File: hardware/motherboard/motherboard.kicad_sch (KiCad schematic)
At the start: 82 parts, among them J1 IMU Connector, J2 JST-VH, J3 JST-VH, J4 JST-PH, J5 USB C 2.0, Q1 TSM7P06CP_ROG, Q2 TSM7P06CP_ROG, SW1 A, SW10 Right, SW11 Left, SW12 Up, SW13 Reset, SW2 B, SW3 X, SW4 Y, SW5 LB, SW6 RB, SW7 Start, SW8 Select, SW9 Down, U1 ESP32-S3-WROOM-1, U2 MCP73831-2-OT, U3 TPS75533KTTRG3, U4 TLV75709PDBV, U5 COM-09032

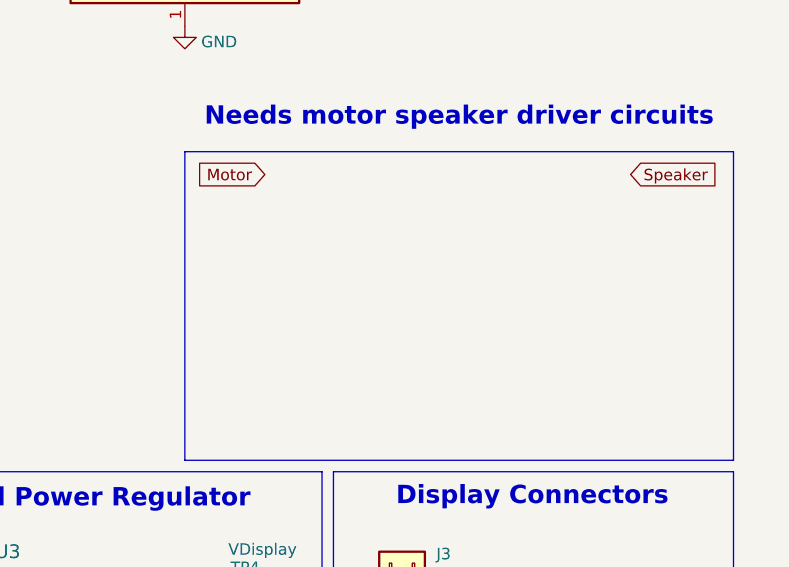
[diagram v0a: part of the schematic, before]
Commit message: Updated Schematic, Added motor/speaker connector
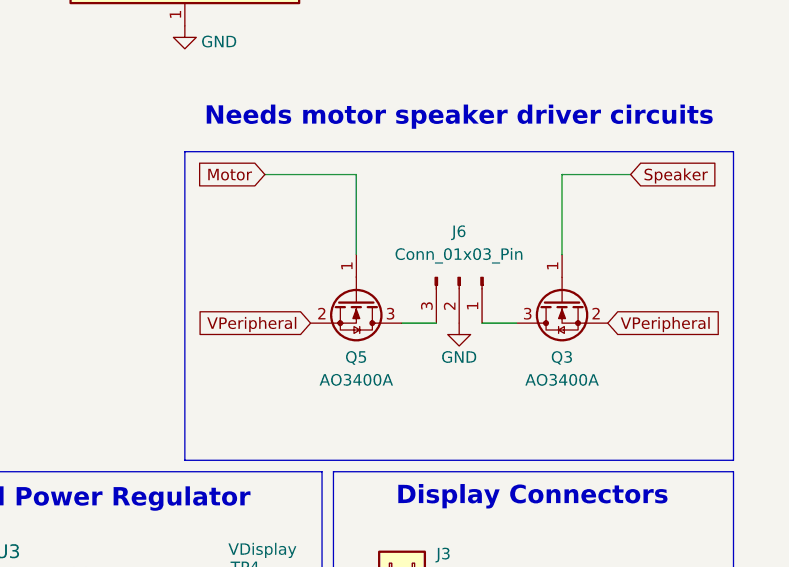
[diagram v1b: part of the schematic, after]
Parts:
- added J6: Conn_01x03_Pin, symbol Connector:Conn_01x03_Pin
- added Q3, Q5: AO3400A, Package_TO_SOT_SMD:SOT-23, symbol Transistor_FET:AO3400A
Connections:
- net GND: now also J6.2 (Pin_2)
- net Motor: now also Q5.1 (G)
- net Speaker: now also Q3.1 (G)
- net VPeripheral: now also Q3.2 (S), Q5.2 (S)
- new net: J6.1 (Pin_1), Q3.3 (D)
- new net: J6.3 (Pin_3), Q5.3 (D)

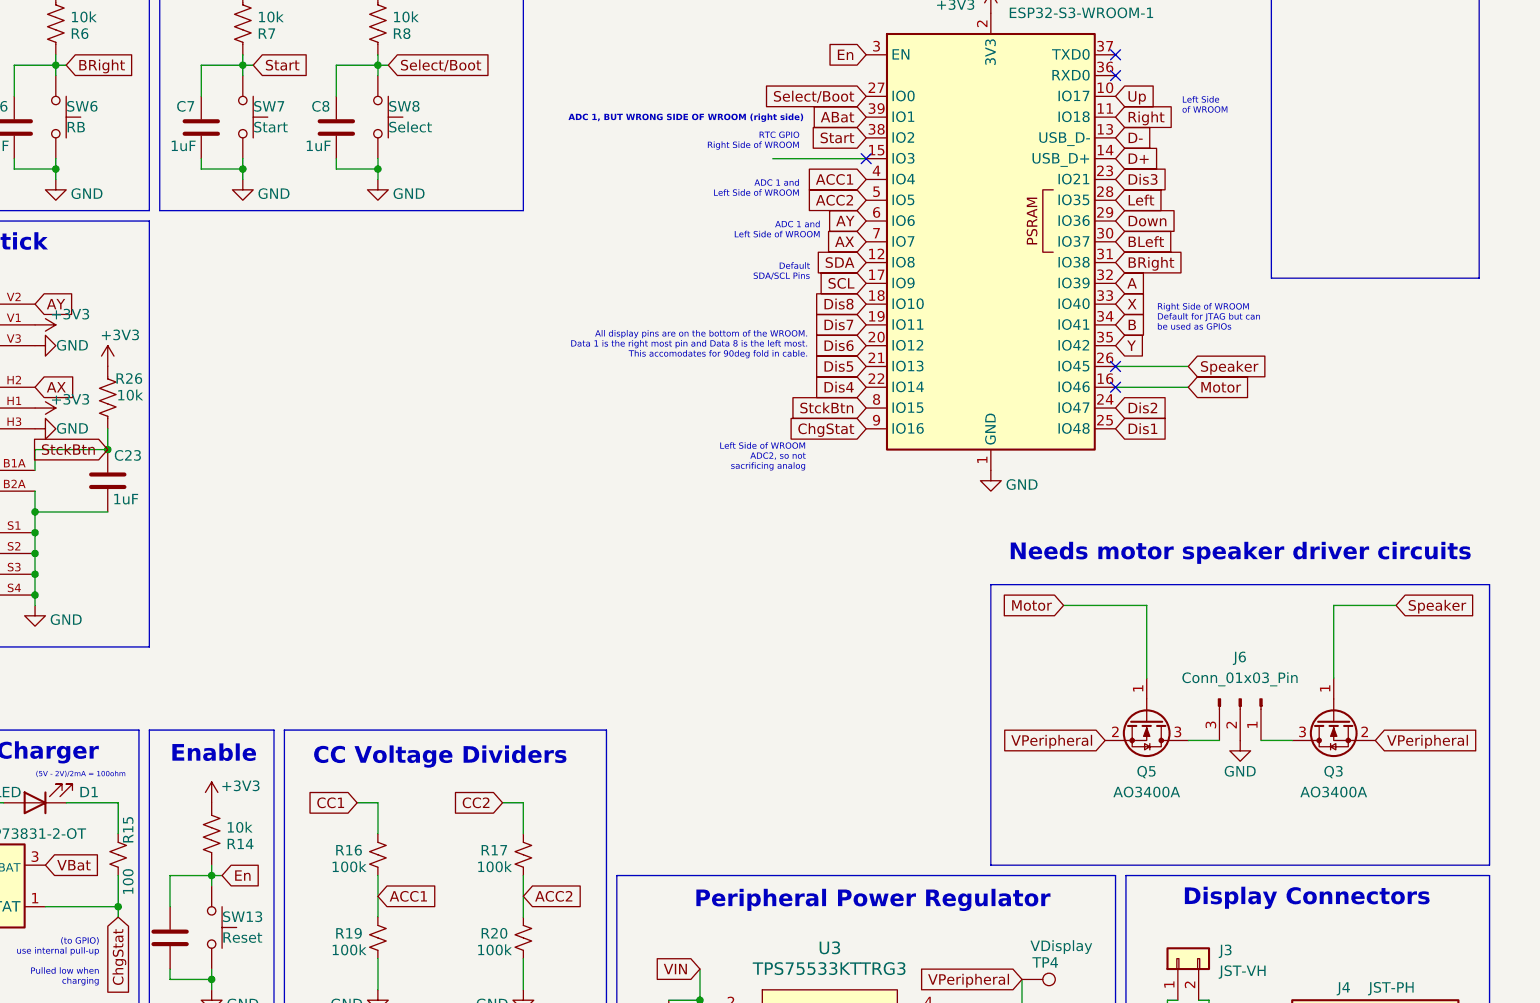
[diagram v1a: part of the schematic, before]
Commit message: Added ucbc 3d model
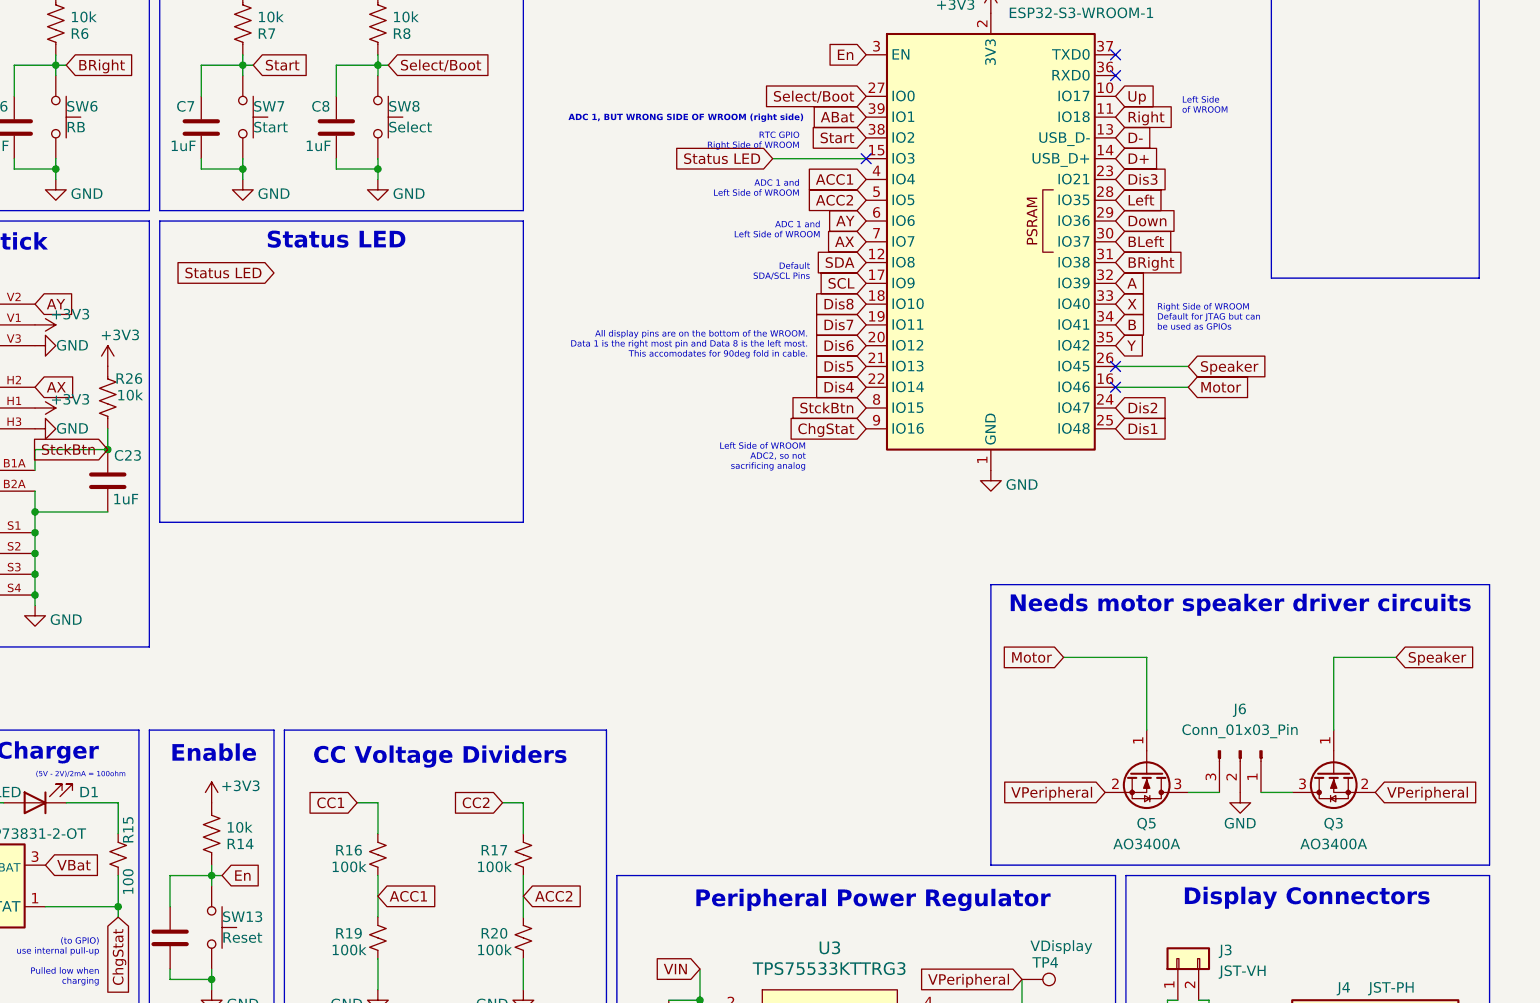
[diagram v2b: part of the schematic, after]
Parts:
- J6: footprint (none) -> Connector_JST:JST_EH_S3B-EH_1x03_P2.50mm_Horizontal
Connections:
- net Status LED: now reaches U1.15 (IO3)
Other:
- note added: "Status LED"
- moved on the sheet: J6, Q3, Q5
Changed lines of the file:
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@@
 	)
 	(rectangle
+		(start 120.65 50.8)
+		(end 165.1 87.63)
+		(stroke
+			(width 0)
+			(type default)
+		)
+		(fill
+			(type none)
+		)
+	)
+	(rectangle
 		(start 81.28 12.7)
 		(end 119.38 49.53)
@@
 	(text "Needs motor speaker driver circuits"
 		(exclude_from_sim no)
-		(at 252.73 91.44 0)
+		(at 252.73 97.79 0)
 		(effects
 			(font
@@
 		)
 	)
+	(text "Status LED"
+		(exclude_from_sim no)
+		(at 142.24 53.34 0)
+		(effects
+			(font
+				(size 2.032 2.032)
+				(thickness 0.6096)
+				(bold yes)
+			)
+		)
+	)
 	(junction
 		(at 127 130.81)
@@
 	(wire
 		(pts
-			(xy 264.16 97.79) (xy 264.16 106.68)
+			(xy 264.16 104.14) (xy 264.16 113.03)
 		)
 		(stroke
@@
 	(wire
 		(pts
-			(xy 255.27 114.3) (xy 259.08 114.3)
+			(xy 255.27 120.65) (xy 259.08 120.65)
 		)
 		(stroke
@@
 	(wire
 		(pts
-			(xy 241.3 97.79) (xy 241.3 106.68)
+			(xy 241.3 104.14) (xy 241.3 113.03)
 		)
 		(stroke
@@
 	(wire
 		(pts
-			(xy 271.78 97.79) (xy 264.16 97.79)
+			(xy 271.78 104.14) (xy 264.16 104.14)
 		)
 		(stroke
@@
 	(wire
 		(pts
-			(xy 231.14 97.79) (xy 241.3 97.79)
+			(xy 231.14 104.14) (xy 241.3 104.14)
 		)
 		(stroke
@@
 	(wire
 		(pts
-			(xy 250.19 114.3) (xy 246.38 114.3)
+			(xy 250.19 120.65) (xy 246.38 120.65)
 		)
 		(stroke
@@
 	(global_label "VPeripheral"
 		(shape input)
-		(at 236.22 114.3 180)
+		(at 236.22 120.65 180)
 		(fields_autoplaced yes)
 		(effects
@@
 		)
 		(property "Intersheetrefs" "${INTERSHEET_REFS}"
-			(at 222.4096 114.3 0)
+			(at 222.4096 120.65 0)
 			(effects
 				(font
@@
 	(global_label "VPeripheral"
 		(shape input)
-		(at 269.24 114.3 0)
+		(at 269.24 120.65 0)
 		(fields_autoplaced yes)
 		(effects
@@
 		)
 		(property "Intersheetrefs" "${INTERSHEET_REFS}"
-			(at 283.0504 114.3 0)
+			(at 283.0504 120.65 0)
 			(effects
 				(font
@@
 		)
 	)
+	(global_label "Status LED"
+		(shape input)
+		(at 195.58 43.18 180)
+		(fields_autoplaced yes)
+		(effects
+			(font
+				(size 1.27 1.27)
+			)
+			(justify right)
+		)
+		(property "Intersheetrefs" "${INTERSHEET_REFS}"
+			(at 182.1931 43.18 0)
+			(effects
+				(font
+					(size 1.27 1.27)
+				)
+				(justify right)
+				(hide yes)
+			)
+		)
+	)
 	(global_label "AY"
 		(shape input)
@@
 	(global_label "Motor"
 		(shape input)
-		(at 231.14 97.79 180)
+		(at 231.14 104.14 180)
 		(fields_autoplaced yes)
 		(effects
@@
 		)
 		(property "Intersheetrefs" "${INTERSHEET_REFS}"
-			(at 222.8935 97.79 0)
+			(at 222.8935 104.14 0)
 			(effects
 				(font
@@
 		)
 	)
+	(global_label "Status LED"
+		(shape input)
+		(at 134.62 57.15 180)
+		(fields_autoplaced yes)
+		(effects
+			(font
+				(size 1.27 1.27)
+			)
+			(justify right)
+		)
+		(property "Intersheetrefs" "${INTERSHEET_REFS}"
+			(at 121.2331 57.15 0)
+			(effects
+				(font
+					(size 1.27 1.27)
+				)
+				(justify right)
+				(hide yes)
+			)
+		)
+	)
 	(global_label "Speaker"
 		(shape input)
-		(at 271.78 97.79 0)
+		(at 271.78 104.14 0)
 		(fields_autoplaced yes)
 		(effects
@@
 		)
 		(property "Intersheetrefs" "${INTERSHEET_REFS}"
-			(at 282.2642 97.79 0)
+			(at 282.2642 104.14 0)
 			(effects
 				(font
@@
 	(symbol
 		(lib_id "Connector:Conn_01x03_Pin")
-		(at 252.73 109.22 270)
+		(at 252.73 115.57 270)
 		(unit 1)
 		(exclude_from_sim no)
@@
 		(fields_autoplaced yes)
 		(property "Reference" "J6"
-			(at 252.73 104.14 90)
+			(at 252.73 110.49 90)
 			(effects
 				(font
@@
 		)
 		(property "Value" "Conn_01x03_Pin"
-			(at 252.73 106.68 90)
+			(at 252.73 113.03 90)
 			(effects
 				(font
@@
 			)
 		)
-		(property "Footprint" ""
-			(at 252.73 109.22 0)
+		(property "Footprint" "Connector_JST:JST_EH_S3B-EH_1x03_P2.50mm_Horizontal"
+			(at 252.73 115.57 0)
 			(effects
 				(font
@@
 		)
 		(property "Datasheet" "~"
-			(at 252.73 109.22 0)
+			(at 252.73 115.57 0)
 			(effects
 				(font
@@
 		)
 		(property "Description" "Generic connector, single row, 01x03, script generated"
-			(at 252.73 109.22 0)
+			(at 252.73 115.57 0)
 			(effects
 				(font
@@
 	(symbol
 		(lib_id "power:GND")
-		(at 252.73 114.3 0)
+		(at 252.73 120.65 0)
 		(mirror y)
 		(unit 1)
@@
 		(dnp no)
 		(property "Reference" "#PWR064"
-			(at 252.73 120.65 0)
+			(at 252.73 127 0)
 			(effects
 				(font
@@
 		)
 		(property "Value" "GND"
-			(at 252.73 118.11 0)
+			(at 252.73 124.46 0)
 			(effects
 				(font
@@
 		)
 		(property "Footprint" ""
-			(at 252.73 114.3 0)
+			(at 252.73 120.65 0)
 			(effects
 				(font
@@
 		)
 		(property "Datasheet" ""
-			(at 252.73 114.3 0)
+			(at 252.73 120.65 0)
 			(effects
 				(font
@@
 		)
 		(property "Description" "Power symbol creates a global label with name \"GND\" , ground"
-			(at 252.73 114.3 0)
+			(at 252.73 120.65 0)
 			(effects
 				(font
@@
 	(symbol
 		(lib_id "Transistor_FET:AO3400A")
-		(at 264.16 111.76 90)
+		(at 264.16 118.11 90)
 		(mirror x)
 		(unit 1)
@@
 		(dnp no)
 		(property "Reference" "Q3"
-			(at 264.16 118.11 90)
+			(at 264.16 124.46 90)
 			(effects
 				(font
@@
 		)
 		(property "Value" "AO3400A"
-			(at 264.16 120.65 90)
+			(at 264.16 127 90)
 			(effects
 				(font
@@
 		)
 		(property "Footprint" "Package_TO_SOT_SMD:SOT-23"
-			(at 266.065 116.84 0)
+			(at 266.065 123.19 0)
 			(effects
 				(font
@@
 		)
 		(property "Datasheet" "http://www.aosmd.com/pdfs/datasheet/AO3400A.pdf"
-			(at 267.97 116.84 0)
+			(at 267.97 123.19 0)
 			(effects
 				(font
@@
 		)
 		(property "Description" "30V Vds, 5.7A Id, N-Channel MOSFET, SOT-23"
-			(at 264.16 111.76 0)
+			(at 264.16 118.11 0)
 			(effects
 				(font
@@
 	(symbol
 		(lib_id "Transistor_FET:AO3400A")
-		(at 241.3 111.76 270)
+		(at 241.3 118.11 270)
 		(unit 1)
 		(exclude_from_sim no)
@@
 		(fields_autoplaced yes)
 		(property "Reference" "Q5"
-			(at 241.3 118.11 90)
+			(at 241.3 124.46 90)
 			(effects
 				(font
@@
 		)
 		(property "Value" "AO3400A"
-			(at 241.3 120.65 90)
+			(at 241.3 127 90)
 			(effects
 				(font
@@
 		)
 		(property "Footprint" "Package_TO_SOT_SMD:SOT-23"
-			(at 239.395 116.84 0)
+			(at 239.395 123.19 0)
 			(effects
 				(font
@@
 		)
 		(property "Datasheet" "http://www.aosmd.com/pdfs/datasheet/AO3400A.pdf"
-			(at 237.49 116.84 0)
+			(at 237.49 123.19 0)
 			(effects
 				(font
@@
 		)
 		(property "Description" "30V Vds, 5.7A Id, N-Channel MOSFET, SOT-23"
-			(at 241.3 111.76 0)
+			(at 241.3 118.11 0)
 			(effects
 				(font

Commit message: Updated Motherboard
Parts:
- added D3: StatusLED, LED_SMD:LED_1206_3216Metric, symbol Device:LED
- added R27: 100, Resistor_SMD:R_0805_2012Metric_Pad1.20x1.40mm_HandSolder, symbol Device:R_Small_US
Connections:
- net GND: now also R27.1
- net Status LED: now also D3.2 (A)
- new net: D3.1 (K), R27.2
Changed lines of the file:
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@@
 	(rectangle
 		(start 120.65 50.8)
-		(end 165.1 87.63)
+		(end 165.1 73.66)
 		(stroke
 			(width 0)
@@
 	(wire
 		(pts
-			(xy 241.3 104.14) (xy 241.3 113.03)
-		)
-		(stroke
-			(width 0)
-			(type default)
-		)
-	)
-	(wire
-		(pts
 			(xy 39.37 82.55) (xy 34.29 82.55)
 		)
@@
 	(wire
 		(pts
+			(xy 152.4 64.77) (xy 152.4 58.42)
+		)
+		(stroke
+			(width 0)
+			(type default)
+		)
+	)
+	(wire
+		(pts
 			(xy 147.32 130.81) (xy 147.32 135.89)
 		)
@@
 	(wire
 		(pts
+			(xy 144.78 58.42) (xy 138.43 58.42)
+		)
+		(stroke
+			(width 0)
+			(type default)
+		)
+	)
+	(wire
+		(pts
 			(xy 107.95 45.72) (xy 107.95 44.45)
 		)
@@
 	(wire
 		(pts
+			(xy 241.3 104.14) (xy 241.3 113.03)
+		)
+		(stroke
+			(width 0)
+			(type default)
+		)
+	)
+	(wire
+		(pts
 			(xy 24.13 31.75) (xy 22.86 31.75)
 		)
@@
 	(global_label "Status LED"
 		(shape input)
-		(at 134.62 57.15 180)
+		(at 138.43 58.42 180)
 		(fields_autoplaced yes)
 		(effects
@@
 		)
 		(property "Intersheetrefs" "${INTERSHEET_REFS}"
-			(at 121.2331 57.15 0)
+			(at 125.0431 58.42 0)
 			(effects
 				(font
@@
 	)
 	(symbol
+		(lib_id "power:GND")
+		(at 152.4 69.85 0)
+		(unit 1)
+		(exclude_from_sim no)
+		(in_bom yes)
+		(on_board yes)
+		(dnp no)
+		(property "Reference" "#PWR062"
+			(at 152.4 76.2 0)
+			(effects
+				(font
+					(size 1.27 1.27)
+				)
+				(hide yes)
+			)
+		)
+		(property "Value" "GND"
+			(at 156.21 71.628 0)
+			(effects
+				(font
+					(size 1.27 1.27)
+				)
+			)
+		)
+		(property "Footprint" ""
+			(at 152.4 69.85 0)
+			(effects
+				(font
+					(size 1.27 1.27)
+				)
+				(hide yes)
+			)
+		)
+		(property "Datasheet" ""
+			(at 152.4 69.85 0)
+			(effects
+				(font
+					(size 1.27 1.27)
+				)
+				(hide yes)
+			)
+		)
+		(property "Description" "Power symbol creates a global label with name \"GND\" , ground"
+			(at 152.4 69.85 0)
+			(effects
+				(font
+					(size 1.27 1.27)
+				)
+				(hide yes)
+			)
+		)
+		(pin "1"
+		)
+		(instances
+			(project "motherboard"
+				(path "/4bd92664-563a-4440-acf2-e22b0a15db62"
+					(reference "#PWR062")
+					(unit 1)
+				)
+			)
+		)
+	)
+	(symbol
 		(lib_id "Device:R_US")
 		(at 39.37 64.77 180)
@@
 	)
 	(symbol
+		(lib_id "Device:R_Small_US")
+		(at 152.4 67.31 180)
+		(unit 1)
+		(exclude_from_sim no)
+		(in_bom yes)
+		(on_board yes)
+		(dnp no)
+		(property "Reference" "R27"
+			(at 153.67 64.262 90)
+			(effects
+				(font
+					(size 1.27 1.27)
+				)
+			)
+		)
+		(property "Value" "100"
+			(at 149.86 69.85 90)
+			(effects
+				(font
+					(size 1.27 1.27)
+				)
+			)
+		)
+		(property "Footprint" "Resistor_SMD:R_0805_2012Metric_Pad1.20x1.40mm_HandSolder"
+			(at 152.4 67.31 0)
+			(effects
+				(font
+					(size 1.27 1.27)
+				)
+				(hide yes)
+			)
+		)
+		(property "Datasheet" "~"
+			(at 152.4 67.31 0)
+			(effects
+				(font
+					(size 1.27 1.27)
+				)
+				(hide yes)
+			)
+		)
+		(property "Description" "Resistor, small US symbol"
+			(at 152.4 67.31 0)
+			(effects
+				(font
+					(size 1.27 1.27)
+				)
+				(hide yes)
+			)
+		)
+		(pin "2"
+		)
+		(pin "1"
+		)
+		(instances
+			(project "motherboard"
+				(path "/4bd92664-563a-4440-acf2-e22b0a15db62"
+					(reference "R27")
+					(unit 1)
+				)
+			)
+		)
+	)
+	(symbol
 		(lib_id "Device:C")
 		(at 34.29 77.47 0)
@@
 					(unit 1)
 				)
+			)
+		)
+	)
+	(symbol
+		(lib_id "Device:LED")
+		(at 148.59 58.42 180)
+		(unit 1)
+		(exclude_from_sim no)
+		(in_bom yes)
+		(on_board yes)
+		(dnp no)
+		(property "Reference" "D3"
+			(at 155.194 57.15 0)
+			(effects
+				(font
+					(size 1.27 1.27)
+				)
+			)
+		)
+		(property "Value" "StatusLED"
+			(at 144.78 62.23 0)
+			(effects
+				(font
+					(size 1.27 1.27)
+				)
+			)
+		)
+		(property "Footprint" "LED_SMD:LED_1206_3216Metric"
+			(at 148.59 58.42 0)
+			(effects
+				(font
+					(size 1.27 1.27)
+				)
+				(hide yes)
+			)
+		)
+		(property "Datasheet" "~"
+			(at 148.59 58.42 0)
+			(effects
+				(font
+					(size 1.27 1.27)
+				)
+				(hide yes)
+			)
+		)
+		(property "Description" "Light emitting diode"
+			(at 148.59 58.42 0)
+			(effects
+				(font
+					(size 1.27 1.27)
+				)
+				(hide yes)
+			)
+		)
+		(property "Sim.Pins" "1=K 2=A"
+			(at 148.59 58.42 0)
+			(effects
+				(font
+					(size 1.27 1.27)
+				)
+				(hide yes)
+			)
+		)
+		(pin "2"
+		)
+		(pin "1"
+		)
+		(instances
+			(project "motherboard"
+				(path "/4bd92664-563a-4440-acf2-e22b0a15db62"
+					(reference "D3")
+					(unit 1)
+				)

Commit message: Routing
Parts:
- removed U5: COM-09032, esp32_handheld:XDCR_COM-09032, symbol esp32_handheld:COM-09032
- added JY1: ~, esp32_handheld:Adafruit_Joycon, symbol esp32_handheld:Joycon
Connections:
- net +3V3: now also JY1.6 (VCC)
- net AX: now also JY1.1 (AD1)
- net AY: now also JY1.4 (AD2)
- net GND: now also C23.1, JY1.2 (GND), JY1.5 (GND); no longer C23.2
- net Right: now also U1.10 (IO17); no longer U1.11 (IO18)
- net StckBtn: now also C23.2, JY1.3 (Switch); no longer C23.1
- net Up: now also U1.11 (IO18); no longer U1.10 (IO17)
- no-connect marks 9 -> 6
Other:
- moved on the sheet: C23, R26
